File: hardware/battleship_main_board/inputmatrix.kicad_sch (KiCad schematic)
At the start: 16 parts

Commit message: Work on main board
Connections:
- net +5V: no longer U?.14 (VCC), U?.14 (VCC), U?.14 (VCC)
- net Button69/ColOut: now also U?.1; no longer U?.4
- net Button80/ColOut: now also U?.1; no longer U?.12
- net Button81/ColOut: now also U?.1; no longer U?.9
- net Button88/ColOut: now also U?.1; no longer U?.4
- net Button92/ColOut: now also U?.1; no longer U?.12
- net Button94/ColOut: now also U?.1; no longer U?.4
- net Button98/ColOut: now also U?.1; no longer U?.9
- net ButtonOut: now also U?.3, U?.3, U?.3, U?.3, U?.3, U?.3, U?.3; no longer U?.11, U?.11, U?.6, U?.6, U?.6, U?.8, U?.8
- net Col1: now also U?.2; no longer U?.5
- net Col2: now also U?.2; no longer U?.10
- net Col3: now also U?.2; no longer U?.13
- net Col5: now also U?.2; no longer U?.5
- net Col6: now also U?.2; no longer U?.10
- net Col7: now also U?.2; no longer U?.13
- net Col9: now also U?.2; no longer U?.5
- net GNDREF: now also U?.1, U?.1, U?.2, U?.2, U?.3, U?.3; no longer U?.10, U?.11, U?.12, U?.13, U?.7 (GND), U?.7 (GND), U?.7 (GND), U?.8, U?.9
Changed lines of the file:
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@@
   (junction (at 161.29 369.57) (diameter 0) (color 0 0 0 0)
   )
-  (junction (at 76.2 386.08) (diameter 0) (color 0 0 0 0)
-  )
   (junction (at 247.65 369.57) (diameter 0) (color 0 0 0 0)
   )
-  (junction (at 76.2 360.68) (diameter 0) (color 0 0 0 0)
-  )
   (junction (at 44.45 379.73) (diameter 0) (color 0 0 0 0)
   )
-  (junction (at 96.52 386.08) (diameter 0) (color 0 0 0 0)
-  )
   (junction (at 204.47 369.57) (diameter 0) (color 0 0 0 0)
   )
@@
   )
   (junction (at 269.24 369.57) (diameter 0) (color 0 0 0 0)
-  )
-  (junction (at 54.61 386.08) (diameter 0) (color 0 0 0 0)
   )
   (junction (at 46.99 386.08) (diameter 0) (color 0 0 0 0)
@@
     (stroke (width 0) (type default) (color 0 0 0 0))
   )
-  (wire (pts (xy 46.99 386.08) (xy 54.61 386.08))
+  (wire (pts (xy 46.99 386.08) (xy 96.52 386.08))
     (stroke (width 0) (type default) (color 0 0 0 0))
   )
@@
     (stroke (width 0) (type default) (color 0 0 0 0))
   )
-  (wire (pts (xy 54.61 360.68) (xy 76.2 360.68))
+  (wire (pts (xy 54.61 360.68) (xy 96.52 360.68))
     (stroke (width 0) (type default) (color 0 0 0 0))
   )
@@
     (stroke (width 0) (type default) (color 0 0 0 0))
   )
-  (wire (pts (xy 54.61 386.08) (xy 76.2 386.08))
-    (stroke (width 0) (type default) (color 0 0 0 0))
-  )
   (wire (pts (xy 213.36 248.92) (xy 222.25 248.92))
     (stroke (width 0) (type default) (color 0 0 0 0))
@@
     (stroke (width 0) (type default) (color 0 0 0 0))
   )
-  (wire (pts (xy 76.2 360.68) (xy 96.52 360.68))
-    (stroke (width 0) (type default) (color 0 0 0 0))
-  )
   (wire (pts (xy 213.36 135.89) (xy 222.25 135.89))
     (stroke (width 0) (type default) (color 0 0 0 0))
@@
   )
   (wire (pts (xy 163.83 300.99) (xy 163.83 311.15))
-    (stroke (width 0) (type default) (color 0 0 0 0))
-  )
-  (wire (pts (xy 76.2 386.08) (xy 96.52 386.08))
     (stroke (width 0) (type default) (color 0 0 0 0))
   )
@@
     (effects (font (size 1.27 1.27)) (justify right))
   )
-  (symbol (lib_id "74xx:74LS08") (at 76.2 373.38 0) (unit 5)
+  (symbol (lib_id "74xx:74LS08") (at 76.2 373.38 0)
     (in_bom yes) (on_board yes) (fields_autoplaced)
     (property "Reference" "U?" (id 0) (at 82.55 372.1099 0)
@@
     (pin "7")
   )
-  (symbol (lib_id "74xx:74LS08") (at 161.29 361.95 270) (unit 2)
+  (symbol (lib_id "74xx:74LS08") (at 161.29 361.95 270)
     (in_bom yes) (on_board yes) (fields_autoplaced)
     (property "Reference" "U?" (id 0) (at 166.37 360.6799 90)
@@
     (pin "6")
   )
-  (symbol (lib_id "74xx:74LS08") (at 312.42 361.95 270) (unit 1)
+  (symbol (lib_id "74xx:74LS08") (at 312.42 361.95 270)
     (in_bom yes) (on_board yes) (fields_autoplaced)
     (property "Reference" "U?" (id 0) (at 317.5 360.6799 90)
@@
     (pin "3")
   )
-  (symbol (lib_id "power:+5V") (at 96.52 360.68 0) (unit 1)
+  (symbol (lib_id "power:+5V") (at 96.52 360.68 0)
     (in_bom yes) (on_board yes) (fields_autoplaced)
     (property "Reference" "#PWR?" (id 0) (at 96.52 364.49 0)
@@
     (pin "1")
   )
-  (symbol (lib_id "74xx:74LS08") (at 269.24 361.95 270) (unit 3)
+  (symbol (lib_id "74xx:74LS08") (at 269.24 361.95 270)
     (in_bom yes) (on_board yes) (fields_autoplaced)
     (property "Reference" "U?" (id 0) (at 274.32 360.6799 90)
@@
     (pin "9")
   )
-  (symbol (lib_id "74xx:74LS08") (at 96.52 373.38 0) (unit 5)
+  (symbol (lib_id "74xx:74LS08") (at 96.52 373.38 0)
     (in_bom yes) (on_board yes) (fields_autoplaced)
     (property "Reference" "U?" (id 0) (at 102.87 372.1099 0)
@@
     (pin "7")
   )
-  (symbol (lib_id "74xx:74LS08") (at 334.01 361.95 270) (unit 2)
+  (symbol (lib_id "74xx:74LS08") (at 334.01 361.95 270)
     (in_bom yes) (on_board yes) (fields_autoplaced)
     (property "Reference" "U?" (id 0) (at 339.09 360.6799 90)
@@
     (pin "6")
   )
-  (symbol (lib_id "74xx:74LS08") (at 290.83 361.95 270) (unit 4)
+  (symbol (lib_id "74xx:74LS08") (at 290.83 361.95 270)
     (in_bom yes) (on_board yes) (fields_autoplaced)
     (property "Reference" "U?" (id 0) (at 295.91 360.6799 90)
@@
     (pin "13")
   )
-  (symbol (lib_id "power:GNDREF") (at 96.52 386.08 0) (unit 1)
+  (symbol (lib_id "power:GNDREF") (at 96.52 386.08 0)
     (in_bom yes) (on_board yes) (fields_autoplaced)
     (property "Reference" "#PWR?" (id 0) (at 96.52 392.43 0)
@@
     (pin "1")
   )
-  (symbol (lib_id "Device:R") (at 334.01 377.19 0) (unit 1)
+  (symbol (lib_id "Device:R") (at 334.01 377.19 0)
     (in_bom yes) (on_board yes) (fields_autoplaced)
     (property "Reference" "R?" (id 0) (at 336.55 375.9199 0)
@@
     (pin "2")
   )
-  (symbol (lib_id "74xx:74LS08") (at 247.65 361.95 270) (unit 2)
+  (symbol (lib_id "74xx:74LS08") (at 247.65 361.95 270)
     (in_bom yes) (on_board yes) (fields_autoplaced)
     (property "Reference" "U?" (id 0) (at 252.73 360.6799 90)
@@
     (pin "6")
   )
-  (symbol (lib_id "74xx:74LS08") (at 204.47 361.95 270) (unit 4)
+  (symbol (lib_id "74xx:74LS08") (at 204.47 361.95 270)
     (in_bom yes) (on_board yes) (fields_autoplaced)
     (property "Reference" "U?" (id 0) (at 209.55 360.6799 90)
@@
     (pin "13")
   )
-  (symbol (lib_id "74xx:74LS08") (at 226.06 361.95 270) (unit 1)
+  (symbol (lib_id "74xx:74LS08") (at 226.06 361.95 270)
     (in_bom yes) (on_board yes) (fields_autoplaced)
     (property "Reference" "U?" (id 0) (at 231.14 360.6799 90)
@@
     (pin "3")
   )
-  (symbol (lib_id "74xx:74LS08") (at 41.91 372.11 90) (unit 4)
+  (symbol (lib_id "74xx:74LS08") (at 41.91 372.11 90)
     (in_bom yes) (on_board yes) (fields_autoplaced)
     (property "Reference" "U?" (id 0) (at 33.02 372.11 0))
@@
     (pin "13")
   )
-  (symbol (lib_id "74xx:74LS08") (at 54.61 373.38 0) (unit 5)
+  (symbol (lib_id "74xx:74LS08") (at 54.61 373.38 0)
     (in_bom yes) (on_board yes) (fields_autoplaced)
     (property "Reference" "U?" (id 0) (at 60.96 372.1099 0)
@@
     (pin "7")
   )
-  (symbol (lib_id "74xx:74LS08") (at 182.88 361.95 270) (unit 3)
+  (symbol (lib_id "74xx:74LS08") (at 182.88 361.95 270)
     (in_bom yes) (on_board yes) (fields_autoplaced)
     (property "Reference" "U?" (id 0) (at 187.96 360.6799 90)
@@
     (pin "9")
   )
-  (symbol (lib_id "74xx:74LS08") (at 29.21 372.11 90) (unit 3)
+  (symbol (lib_id "74xx:74LS08") (at 29.21 372.11 90)
     (in_bom yes) (on_board yes) (fields_autoplaced)
     (property "Reference" "U?" (id 0) (at 20.32 372.11 0))
@@
     (pin "9")
   )
-  (symbol (lib_id "74xx:74LS08") (at 139.7 361.95 270) (unit 1)
+  (symbol (lib_id "74xx:74LS08") (at 139.7 361.95 270)
     (in_bom yes) (on_board yes) (fields_autoplaced)
     (property "Reference" "U?" (id 0) (at 144.78 360.6799 90)
@@
     (pin "3")
   )
-  (symbol (lib_id "power:GNDREF") (at 334.01 381 0) (unit 1)
+  (symbol (lib_id "power:GNDREF") (at 334.01 381 0)
     (in_bom yes) (on_board yes) (fields_autoplaced)
     (property "Reference" "#PWR?" (id 0) (at 334.01 387.35 0)

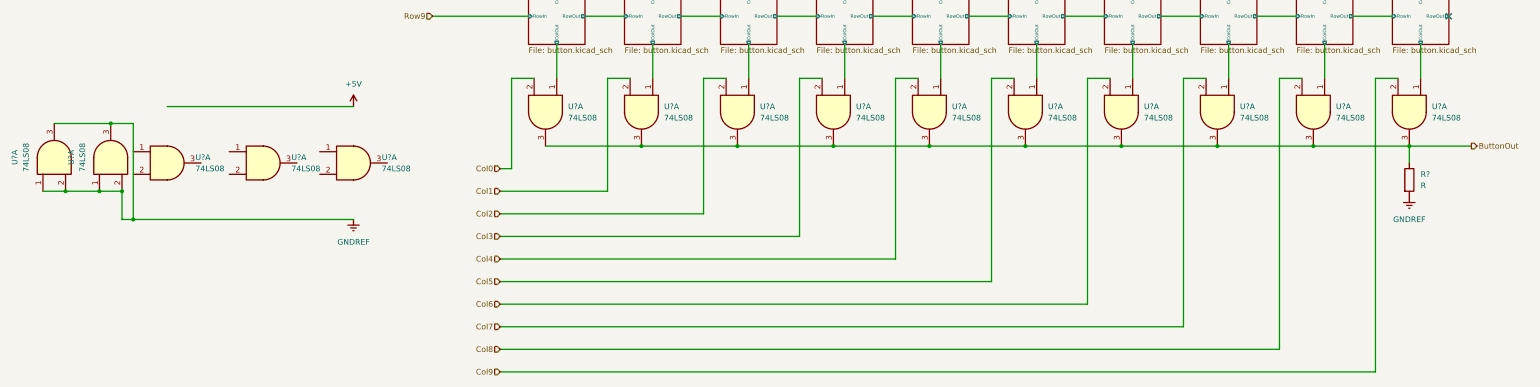
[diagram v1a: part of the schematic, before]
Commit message: Got schematic to place that can be turned into a ratsnest
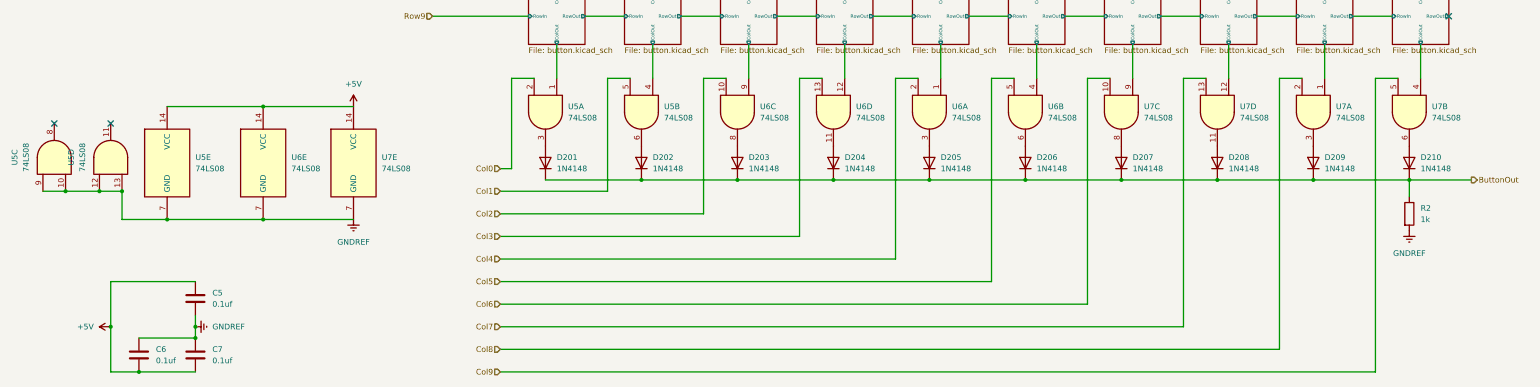
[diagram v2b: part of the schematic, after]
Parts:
- added C5, C6, C7: 0.1uf, Capacitor_THT:C_Disc_D3.0mm_W1.6mm_P2.50mm, symbol Device:C
- added D201, D202, D203, D204, D205, D206, D207, D208, D209, D210: 1N4148, Diode_THT:D_DO-35_SOD27_P7.62mm_Horizontal, symbol Diode:1N4148
- R2: renamed from R?; value R -> 1k; footprint (none) -> Resistor_THT:R_Axial_DIN0207_L6.3mm_D2.5mm_P10.16mm_Horizontal
- U5, U6, U7: renamed from U?; footprint (none) -> Package_DIP:DIP-14_W7.62mm
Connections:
- net +5V: now also U5.14 (VCC), U6.14 (VCC), U7.14 (VCC), C5.1, C6.2, C7.2
- net Button69/ColOut: now also U6.4; no longer U6.1
- net Button80/ColOut: now also U7.12; no longer U7.1
- net Button81/ColOut: now also U7.9; no longer U7.1
- net Button88/ColOut: now also U7.4; no longer U7.1
- net Button92/ColOut: now also U6.12; no longer U6.1
- net Button94/ColOut: now also U5.4; no longer U5.1
- net Button98/ColOut: now also U6.9; no longer U6.1
- net ButtonOut: now also D201.1 (K), D202.1 (K), D203.1 (K), D204.1 (K), D205.1 (K), D206.1 (K), D207.1 (K), D208.1 (K), D209.1 (K), D210.1 (K); no longer U5.3, U5.3, U6.3, U6.3, U6.3, U6.3, U7.3, U7.3, U7.3, U7.3
- net Col1: now also U5.5; no longer U5.2
- net Col2: now also U6.10; no longer U6.2
- net Col3: now also U6.13; no longer U6.2
- net Col5: now also U6.5; no longer U6.2
- net Col6: now also U7.10; no longer U7.2
- net Col7: now also U7.13; no longer U7.2
- net Col9: now also U7.5; no longer U7.2
- net GNDREF: now also U5.10, U5.12, U5.13, U5.7 (GND), U5.9, U6.7 (GND), U7.7 (GND), C5.2, C6.1, C7.1; no longer U5.1, U5.1, U5.2, U5.2, U5.3, U5.3
- new net: D207.2 (A), U7.8
- new net: D209.2 (A), U7.3
- new net: D208.2 (A), U7.11
- new net: D202.2 (A), U5.6
- new net: D206.2 (A), U6.6
- new net: D201.2 (A), U5.3
- new net: D210.2 (A), U7.6
- new net: D203.2 (A), U6.8
- new net: D204.2 (A), U6.11
- new net: D205.2 (A), U6.3
- no-connect marks 20 -> 22
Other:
- moved on the sheet: R2

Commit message: Fixed annotations so that button rows are in order
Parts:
- renumbered D201 to D101, D202 to D102, D203 to D103, D204 to D104, D205 to D105, D206 to D106, D207 to D107, D208 to D108, D209 to D109, D210 to D110, U6 to U5, U7 to U6, U5 to U7
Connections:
- net Button69/ColOut renamed Button Row10/ColumnOut5
- net Button70/ColOut renamed Button Row10/ColumnOut4
- net Button79/ColOut renamed Button Row10/ColumnOut8
- net Button80/ColOut renamed Button Row10/ColumnOut7
- net Button81/ColOut renamed Button Row10/ColumnOut6
- net Button88/ColOut renamed Button Row10/ColumnOut9
- net Button92/ColOut renamed Button Row10/ColumnOut3
- net Button94/ColOut renamed Button Row10/ColumnOut1
- net Button97/ColOut renamed Button Row10/ColumnOut0
- net Button98/ColOut renamed Button Row10/ColumnOut2
- no-connect marks 22 -> 12
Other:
- removed sheet Button
- removed sheet Button1
- removed sheet Button10
- removed sheet Button11
- removed sheet Button12
- removed sheet Button13
- removed sheet Button14
- removed sheet Button15
- removed sheet Button16
- removed sheet Button17
- removed sheet Button18
- removed sheet Button19
- removed sheet Button2
- removed sheet Button20
- removed sheet Button21
- removed sheet Button22
- removed sheet Button23
- removed sheet Button24
- removed sheet Button25
- removed sheet Button26
- removed sheet Button27
- removed sheet Button28
- removed sheet Button29
- removed sheet Button3
- removed sheet Button30
- removed sheet Button31
- removed sheet Button32
- removed sheet Button33
- removed sheet Button34
- removed sheet Button35
- removed sheet Button36
- removed sheet Button37
- removed sheet Button38
- removed sheet Button39
- removed sheet Button4
- removed sheet Button40
- removed sheet Button41
- removed sheet Button42
- removed sheet Button43
- removed sheet Button44
- removed sheet Button45
- removed sheet Button46
- removed sheet Button47
- removed sheet Button48
- removed sheet Button49
- removed sheet Button5
- removed sheet Button50
- removed sheet Button51
- removed sheet Button52
- removed sheet Button53
- removed sheet Button54
- removed sheet Button55
- removed sheet Button56
- removed sheet Button57
- removed sheet Button58
- removed sheet Button59
- removed sheet Button6
- removed sheet Button60
- removed sheet Button61
- removed sheet Button62
- removed sheet Button63
- removed sheet Button64
- removed sheet Button65
- removed sheet Button66
- removed sheet Button67
- removed sheet Button68
- removed sheet Button69
- removed sheet Button7
- removed sheet Button70
- removed sheet Button71
- removed sheet Button72
- removed sheet Button73
- removed sheet Button74
- removed sheet Button75
- removed sheet Button76
- removed sheet Button77
- removed sheet Button78
- removed sheet Button79
- removed sheet Button8
- removed sheet Button80
- removed sheet Button81
- removed sheet Button82
- removed sheet Button83
- removed sheet Button84
- removed sheet Button85
- removed sheet Button86
- removed sheet Button87
- removed sheet Button88
- removed sheet Button89
- removed sheet Button9
- removed sheet Button90
- removed sheet Button91
- removed sheet Button92
- removed sheet Button93
- removed sheet Button94
- removed sheet Button95
- removed sheet Button96
- removed sheet Button97
- removed sheet Button98
- removed sheet Button99
- added sheet Button Row1 (button_row.kicad_sch)
- added sheet Button Row10 (button_row.kicad_sch)
- added sheet Button Row2 (button_row.kicad_sch)
- added sheet Button Row3 (button_row.kicad_sch)
- added sheet Button Row4 (button_row.kicad_sch)
- added sheet Button Row5 (button_row.kicad_sch)
- added sheet Button Row6 (button_row.kicad_sch)
- added sheet Button Row7 (button_row.kicad_sch)
- added sheet Button Row8 (button_row.kicad_sch)
- added sheet Button Row9 (button_row.kicad_sch)
- moved on the sheet: C5, C6, C7, D101, D102, D103, D104, D105, D106, D107, D108, D109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
